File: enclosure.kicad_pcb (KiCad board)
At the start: 2 copper layers, 100 x 220 mm, 188 parts, among them J101 Conn_01x06_Socket, J102 Conn_01x02_Socket, J103 Conn_01x02_Socket, J104 Conn_01x02_Socket, J105 Conn_01x02_Socket, Q1001 DPLS350E, U1001 MC7805, U1002 MC7812, U101 4041, U201 Si8641BD-B-IS2, U202 R05C05TE05S, U301 SN74LVC1G04DBVR, U302 AD567xR, U401 LTC6992IS6-1, U501 LTC6992IS6-1, U601 LTC6992IS6-1, U701 VNH7070ASTR, U801 VNH7070ASTR, U901 VNH7070ASTR

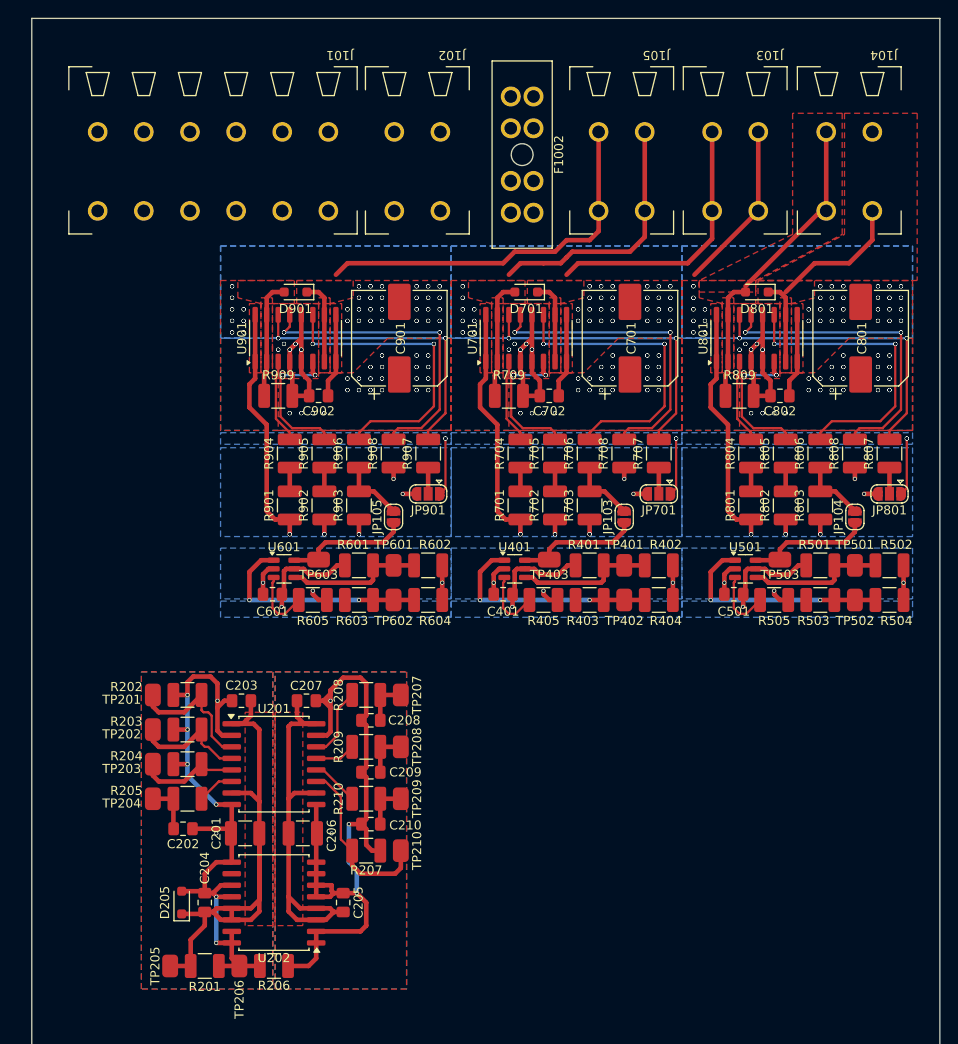
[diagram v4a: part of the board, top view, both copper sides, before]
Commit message: fix zone nets
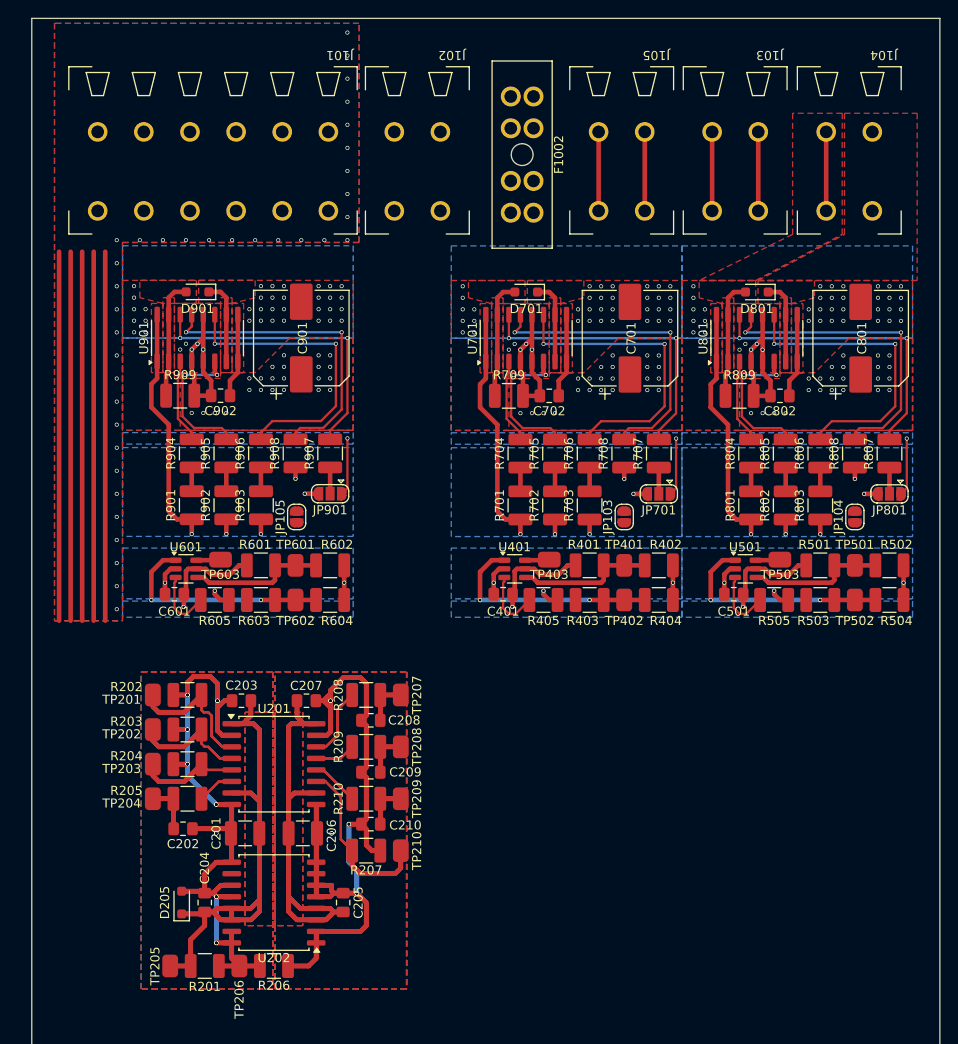
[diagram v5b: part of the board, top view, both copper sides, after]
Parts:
- moved C902 10.8 mm to (170.8, 81.5)
- moved JP901 10.8 mm to (182.9, 92.3)
- moved R907 10.8 mm to (182.9, 87.9)
- moved R908 10.8 mm to (179.0, 87.9)
- moved C901 10.8 mm to (179.7, 75.2)
- moved D901 10.8 mm to (168.2, 70.1)
- moved R901 10.8 mm to (167.6, 93.6)
- moved R902 10.8 mm to (171.4, 93.6)
- moved R903 10.8 mm to (175.2, 93.6)
- moved R904 10.8 mm to (167.6, 87.9)
- moved R905 10.8 mm to (171.4, 87.9)
- moved R906 10.8 mm to (175.2, 87.9)
- moved R909 10.8 mm to (166.3, 81.5)
- moved U901 10.8 mm to (168.2, 75.2)
- moved R602 10.8 mm to (182.9, 100.2)
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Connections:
- net Net-(JP701-C) renamed /full-bridge/sel0_in
- net Net-(JP801-C) renamed /full-bridge1/sel0_in
- net Net-(JP901-C) renamed /full-bridge2/sel0_in
- net Net-(U201-A4) renamed /digital-interface/sdo_iso_pin
- net Net-(U201-B1) renamed /digital-interface/~{cs_pin}
- net Net-(U201-B2) renamed /digital-interface/sckl_pin
- net Net-(U201-B3) renamed /digital-interface/sdi_pin
- net Net-(U701-CS) renamed /full-bridge/cs
- net Net-(U701-IN_A) renamed /full-bridge/in_a
- net Net-(U701-IN_B) renamed /full-bridge/in_b
- net Net-(U701-PWM) renamed /full-bridge/pwm
- net Net-(U701-SEL0) renamed /full-bridge/sel0
- net Net-(U801-CS) renamed /full-bridge1/cs
- net Net-(U801-IN_A) renamed /full-bridge1/in_a
- net Net-(U801-IN_B) renamed /full-bridge1/in_b
- net Net-(U801-PWM) renamed /full-bridge1/pwm
- net Net-(U801-SEL0) renamed /full-bridge1/sel0
- net Net-(U901-CS) renamed /full-bridge2/cs
- net Net-(U901-IN_A) renamed /full-bridge2/in_a
- net Net-(U901-IN_B) renamed /full-bridge2/in_b
- net Net-(U901-PWM) renamed /full-bridge2/pwm
- net Net-(U901-SEL0) renamed /full-bridge2/sel0
- R403 pad 1: /dac_ch_0 -> /pwm/mod_pin
- R404 pad 2: /dac_ch_0 -> /pwm/mod_pin
- R503 pad 1: /dac_ch_1 -> /pwm1/mod_pin
- R504 pad 2: /dac_ch_1 -> /pwm1/mod_pin
- R603 pad 1: /dac_ch_2 -> /pwm2/mod_pin
- R604 pad 2: /dac_ch_2 -> /pwm2/mod_pin
- TP402 pad 1: /dac_ch_0 -> /pwm/mod_pin
- TP502 pad 1: /dac_ch_1 -> /pwm1/mod_pin
- TP602 pad 1: /dac_ch_2 -> /pwm2/mod_pin
- U401 pad 1: /dac_ch_0 -> /pwm/mod_pin
- U501 pad 1: /dac_ch_1 -> /pwm1/mod_pin
- U601 pad 1: /dac_ch_2 -> /pwm2/mod_pin
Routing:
- net (no net): track 0.00 -> 203.2 mm
- net GND: track 235.5 -> 314.7 mm, vias 241 -> 134
- net GNDI: track 73.4 -> 146.9 mm, vias 8 -> 52
- net +5VI: track 63.5 -> 126.9 mm
- net +5VA_digital-interface: track 43.4 -> 86.9 mm
- net /fan_+: track 54.9 -> 21.8 mm
- net /pwm2/mod_pin: track 0.00 -> 24.4 mm, vias 0 -> 2
- net /pwm1/mod_pin: track 0.00 -> 24.4 mm, vias 0 -> 2
- net /dac_ch_1: track 24.4 -> 0.00 mm, vias 2 -> 0
- net /pwm/mod_pin: track 0.00 -> 24.4 mm, vias 0 -> 2
- net /dac_ch_2: track 24.4 -> 0.00 mm, vias 2 -> 0
- net /dac_ch_0: track 24.4 -> 0.00 mm, vias 2 -> 0
- net /heater_+: track 42.5 -> 21.8 mm
- net /fan_-: track 37.5 -> 17.9 mm
- net /digital-interface/SDO: track 19.4 -> 38.8 mm
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- added copper zone on F.Cu, net +5VA_digital-interface
- added copper zone on B.Cu, net GNDI
- removed copper zone on F.Cu, net +5VA_full-bridge
- removed copper zone on B.Cu, net /peltier_+
- removed copper zone on B.Cu, net /pwm1/div

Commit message: fix netnaming collsion
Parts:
- moved F1002 20.9 mm to (188.8, 61.4), turned to 90 degrees
- moved J102 7.50 mm to (202.5, 61.2)
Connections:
- D1001 pad 2: +24V -> /power/IN
- F1002 pad 2: +24V -> /power/IN
- J102 pad 2: +24V -> /power/IN
- TP1001 pad 1: +24V -> /power/IN
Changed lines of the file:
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@@
 	(net 106 "/full-bridge2/sel0")
 	(net 107 "/full-bridge2/cs")
+	(net 108 "/power/IN")
 	(footprint "enclosure:TP_0805_2012Metric"
 		(layer "F.Cu")
@@
 	(footprint "enclosure:FuseHolder_Blade_ATO_Littelfuse_FLR_178.6165"
 		(layer "F.Cu")
-		(at 205.25 48.6 -90)
+		(at 188.75 61.4 90)
 		(descr "Littelfuse fuse holder for ATO/FKS blade fuses, 80V, vertical, 20 x 6mm, PCB thickness up to 1.5mm, http://www.littelfuse.com/~/media/commercial-vehicle/datasheets/automotive-fuse-holders/ato/littelfuse-fuse-holder-ato-flr-pcb-datasheet.pdf")
 		(tags "ATO FKS blade fuse holder")
 		(property "Reference" "F1002"
-			(at 6.4 -2.8 90)
+			(at 6.4 -2.8 270)
 			(layer "F.SilkS")
 			(effects
@@
 		)
 		(property "Value" "Fuse_Socket"
-			(at 6.4 5.4 -90)
+			(at 6.4 5.4 90)
 			(unlocked yes)
 			(layer "F.Fab")
@@
 		)
 		(property "Footprint" "enclosure:FuseHolder_Blade_ATO_Littelfuse_FLR_178.6165"
-			(at 0 0 -90)
+			(at 0 0 90)
 			(unlocked yes)
 			(layer "F.Fab")
@@
 		)
 		(property "Datasheet" "./datasheet/178.6165.0002.pdf"
-			(at 0 0 -90)
+			(at 0 0 90)
 			(unlocked yes)
 			(layer "F.Fab")
@@
 		)
 		(property "Description" "Fuse"
-			(at 0 0 -90)
+			(at 0 0 90)
 			(unlocked yes)
 			(layer "F.Fab")
@@
 		)
 		(property "MPN" "178.6165.0002"
-			(at 0 0 -90)
+			(at 0 0 90)
 			(unlocked yes)
 			(layer "F.Fab")
@@
 		)
 		(property "VPN" "576-178.6165.0002"
-			(at 0 0 -90)
+			(at 0 0 90)
 			(unlocked yes)
 			(layer "F.Fab")
@@
 		(attr through_hole)
 		(fp_line
-			(start -3.91 4.56)
-			(end -3.91 -2.06)
+			(start 16.71 -2.06)
+			(end 16.71 4.56)
 			(stroke
 				(width 0.12)
@@
 		)
 		(fp_line
-			(start 16.71 4.56)
-			(end -3.91 4.56)
+			(start -3.91 -2.06)
+			(end 16.71 -2.06)
 			(stroke
 				(width 0.12)
@@
 		)
 		(fp_line
-			(start -3.91 -2.06)
-			(end 16.71 -2.06)
+			(start 16.71 4.56)
+			(end -3.91 4.56)
 			(stroke
 				(width 0.12)
@@
 		)
 		(fp_line
-			(start 16.71 -2.06)
-			(end 16.71 4.56)
+			(start -3.91 4.56)
+			(end -3.91 -2.06)
 			(stroke
 				(width 0.12)
@@
 		)
 		(fp_line
-			(start -4.1 4.75)
-			(end -4.1 -2.25)
+			(start 16.9 -2.25)
+			(end 16.9 4.75)
 			(stroke
 				(width 0.05)
@@
 		)
 		(fp_line
-			(start 16.9 4.75)
-			(end -4.1 4.75)
+			(start -4.1 -2.25)
+			(end 16.9 -2.25)
 			(stroke
 				(width 0.05)
@@
 		)
 		(fp_line
-			(start -4.1 -2.25)
-			(end 16.9 -2.25)
+			(start 16.9 4.75)
+			(end -4.1 4.75)
 			(stroke
 				(width 0.05)
@@
 		)
 		(fp_line
-			(start 16.9 -2.25)
-			(end 16.9 4.75)
+			(start -4.1 4.75)
+			(end -4.1 -2.25)
 			(stroke
 				(width 0.05)
@@
 		)
 		(fp_line
-			(start -3.6 4.25)
-			(end -3.6 -1.75)
+			(start 16.4 -1.75)
+			(end 16.4 4.25)
 			(stroke
 				(width 0.1)
@@
 		)
 		(fp_line
-			(start 16.4 4.25)
-			(end -3.6 4.25)
+			(start -3.6 -1.75)
+			(end 16.4 -1.75)
 			(stroke
 				(width 0.1)
@@
 		)
 		(fp_line
-			(start -3.6 -1.75)
-			(end 16.4 -1.75)
+			(start 16.4 4.25)
+			(end -3.6 4.25)
 			(stroke
 				(width 0.1)
@@
 		)
 		(fp_line
-			(start 16.4 -1.75)
-			(end 16.4 4.25)
+			(start -3.6 4.25)
+			(end -3.6 -1.75)
 			(stroke
 				(width 0.1)
@@
 		)
 		(fp_text user "${REFERENCE}"
-			(at 6.4 1.25 90)
+			(at 6.4 1.25 270)
 			(layer "F.Fab")
 			(effects
@@
 		)
 		(pad "" np_thru_hole circle
-			(at 6.4 1.25 270)
+			(at 6.4 1.25 90)
 			(size 2.4 2.4)
 			(drill 2.4)
@@
 		)
 		(pad "1" thru_hole circle
-			(at 0 0 270)
+			(at 0 0 90)
 			(size 2.2 2.2)
 			(drill 1.4)
@@
 		)
 		(pad "1" thru_hole circle
-			(at 0 2.5 270)
+			(at 0 2.5 90)
 			(size 2.2 2.2)
 			(drill 1.4)
@@
 		)
 		(pad "1" thru_hole circle
-			(at 3.5 0 270)
+			(at 3.5 0 90)
 			(size 2.2 2.2)
 			(drill 1.4)
@@
 		)
 		(pad "1" thru_hole circle
-			(at 3.5 2.5 270)
+			(at 3.5 2.5 90)
 			(size 2.2 2.2)
 			(drill 1.4)
@@
 		)
 		(pad "2" thru_hole circle
-			(at 9.3 0 270)
+			(at 9.3 0 90)
 			(size 2.2 2.2)
 			(drill 1.4)
 			(layers "*.Cu" "*.Mask")
 			(remove_unused_layers no)
-			(net 15 "+24V")
+			(net 108 "/power/IN")
 			(pintype "passive")
 		)
 		(pad "2" thru_hole circle
-			(at 9.3 2.5 270)
+			(at 9.3 2.5 90)
 			(size 2.2 2.2)
 			(drill 1.4)
 			(layers "*.Cu" "*.Mask")
 			(remove_unused_layers no)
-			(net 15 "+24V")
+			(net 108 "/power/IN")
 			(pintype "passive")
 		)
 		(pad "2" thru_hole circle
-			(at 12.8 0 270)
+			(at 12.8 0 90)
 			(size 2.2 2.2)
 			(drill 1.4)
 			(layers "*.Cu" "*.Mask")
 			(remove_unused_layers no)
-			(net 15 "+24V")
+			(net 108 "/power/IN")
 			(pintype "passive")
 		)
 		(pad "2" thru_hole circle
-			(at 12.8 2.5 270)
+			(at 12.8 2.5 90)
 			(size 2.2 2.2)
 			(drill 1.4)
 			(layers "*.Cu" "*.Mask")
 			(remove_unused_layers no)
-			(net 15 "+24V")
+			(net 108 "/power/IN")
 			(pintype "passive")
 		)
@@
 			(layers "F.Cu" "F.Paste" "F.Mask")
 			(roundrect_rratio 0.243902)
-			(net 15 "+24V")
+			(net 108 "/power/IN")
 			(pinfunction "1")
 			(pintype "passive")
@@
 			(layers "F.Cu" "F.Paste" "F.Mask")
 			(roundrect_rratio 0.25)
-			(net 15 "+24V")
+			(net 108 "/power/IN")
 			(pinfunction "A2")
 			(pintype "passive")
@@
 	(footprint "enclosure:PhoenixContact_TDPT_2,5_2-SP-5,08_1x02_P5.08mm_Horizontal"
 		(layer "F.Cu")
-		(at 195 61.2 180)
+		(at 202.5 61.2 180)
 		(property "Reference" "J102"
 			(at -1.27 17.145 180)
@@
 			(layers "*.Cu" "*.Mask")
 			(remove_unused_layers no)
-			(net 15 "+24V")
+			(net 108 "/power/IN")
 			(pinfunction "Pin_2")
 			(pintype "passive")
@@
 			(layers "*.Cu" "*.Mask")
 			(remove_unused_layers no)
-			(net 15 "+24V")
+			(net 108 "/power/IN")
 			(pinfunction "Pin_2")
 			(pintype "passive")
@@
 			)
 		)
+	)
+	(zone
+		(net 2)
+		(net_name "GND")
+		(layers "F&B.Cu")
+		(hatch edge 0.5)
+		(priority 2)
+		(connect_pads
+			(clearance 0.254)
+		)
+		(min_thickness 0.254)
+		(filled_areas_thickness no)
+		(fill yes
+			(thermal_gap 0.254)
+			(thermal_bridge_width 0.508)
+		)
+		(polygon
+			(pts
+				(xy 150 40) (xy 250 40) (xy 250 260) (xy 150 260)
+			)
+		)

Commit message: add power sub-layout
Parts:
- removed TP1003, TP1004, TP1005, TP1006: ~, enclosure:TP_0805_2012Metric
- moved C101 278.0 mm to (277.0, 161.6)
- moved JP101 278.0 mm to (271.8, 161.9)
- moved JP102 278.0 mm to (271.8, 165.7)
- moved U101 278.0 mm to (264.7, 165.4)
- moved U1002 137.4 mm to (231.8, 140.6)
- moved U1001 130.1 mm to (231.8, 115.2)
- moved D1004 124.1 mm to (223.5, 140.6), turned to -90 degrees
- moved JP1001 123.7 mm to (223.2, 120.9), turned to -90 degrees
- moved R1001 119.3 mm to (221.9, 136.2)
- moved JP1002 119.2 mm to (219.7, 120.9), turned to -90 degrees
- moved JP1004 118.5 mm to (223.2, 109.5), turned to 90 degrees
- moved C1005 117.0 mm to (227.9, 146.3), turned to 180 degrees
- moved D1003 116.4 mm to (223.5, 115.2), turned to -90 degrees
- moved JP1003 115.6 mm to (219.7, 109.5), turned to 90 degrees
- moved TP1009 107.6 mm to (219.7, 143.2)
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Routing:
- net (no net): track 203.2 -> 0.00 mm
- net +12VA: track 18.1 -> 131.8 mm, vias 28 -> 29
- net +24V: track 36.3 -> 141.9 mm, vias 56 -> 79
- net GND: track 314.7 -> 244.2 mm, vias 134 -> 129
- net +5VI: track 126.9 -> 63.5 mm
- net /digital-interface/SDO_ISO: track 11.1 -> 68.0 mm
- net /digital-interface/SDI_ISO: track 22.5 -> 69.3 mm
- net +5VA_digital-interface: track 86.9 -> 43.4 mm
- net /power/IN: track 0.00 -> 40.5 mm
- net /digital-interface/SCKL_ISO: track 26.4 -> 66.9 mm
- net /digital-interface/~{CS_ISO}: track 31.3 -> 65.4 mm
- net +5VA: track 0.00 -> 27.7 mm
- net +5VA_full-bridge: track 19.0 -> 41.6 mm, vias 3 -> 4
- net Net-(D1004-K): track 0.00 -> 20.9 mm
- net /digital-interface/SDO: track 38.8 -> 19.4 mm
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- added copper zone on B.Cu, net /power/IN
- added copper zone on F.Cu, net /power/IN
- removed copper zone on F.Cu, net +5VA_digital-interface
